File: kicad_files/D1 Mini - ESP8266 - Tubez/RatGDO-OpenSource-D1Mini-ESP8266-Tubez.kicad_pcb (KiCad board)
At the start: 2 copper layers, 51.8 x 65.8 mm, 24 parts, among them J1 Screw_Terminal_01x03, J2 Conn_01x11, J3 Screw_Terminal_01x02, Q1 2N7002, Q2 AO3400A, Q3 AO3400A, Q4 AO3400A, U1 WeMos_D1_mini, U2 K7805-500R3

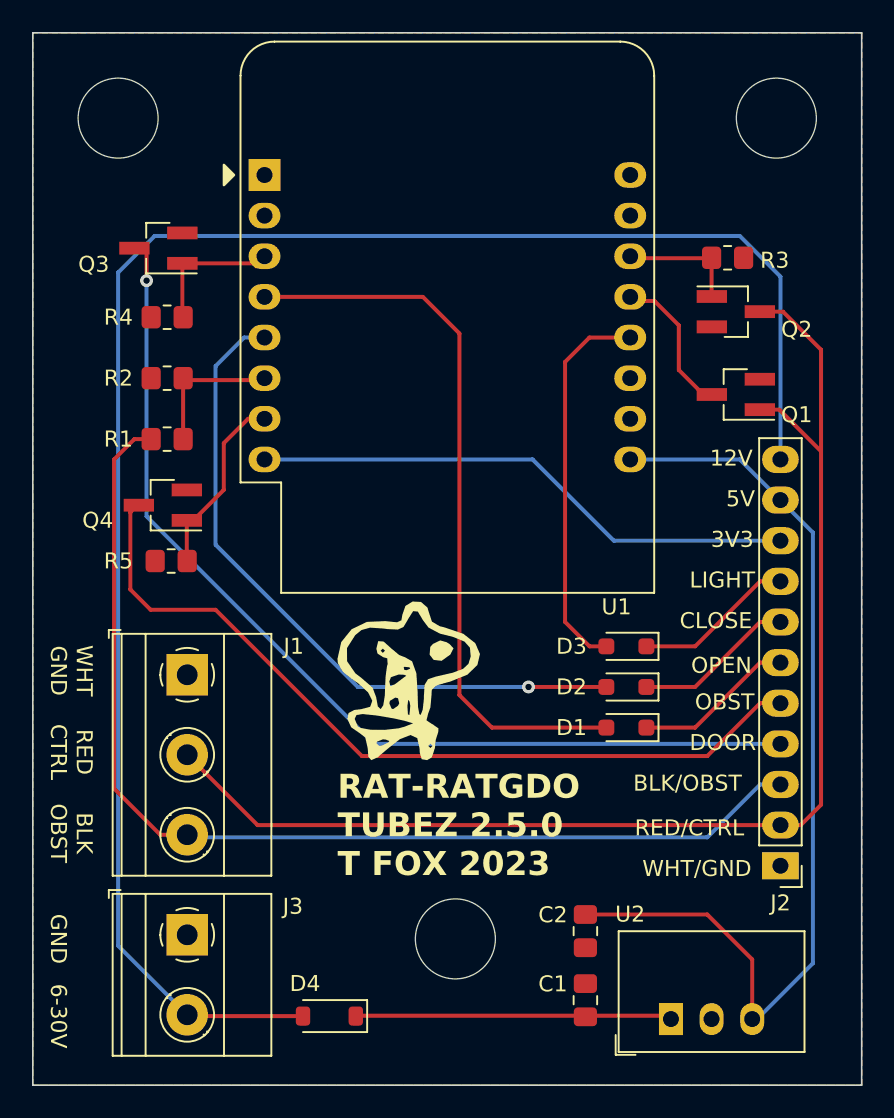
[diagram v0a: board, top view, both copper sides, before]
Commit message: Change angled track intersection to 90
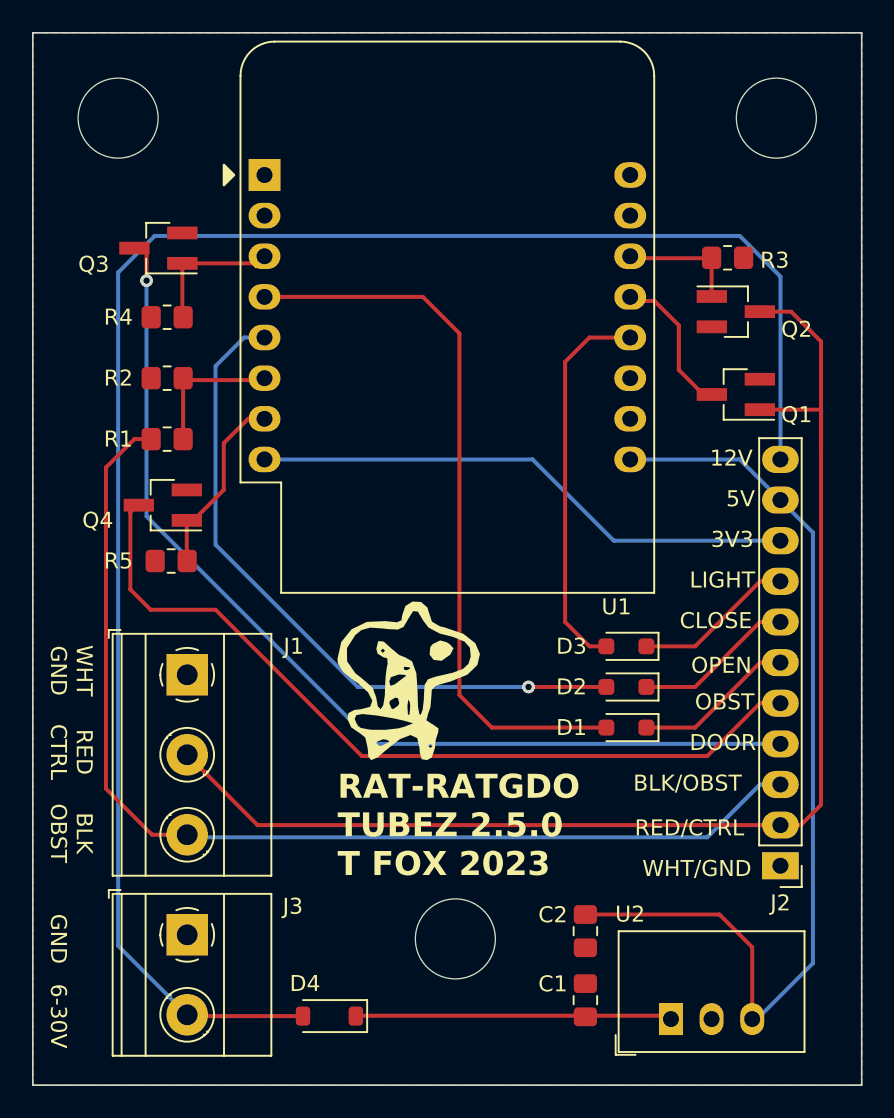
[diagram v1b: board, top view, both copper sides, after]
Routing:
- net RED/CTRL: track 81.3 -> 83.1 mm
- net BLK/OBST: track 65.7 -> 66.4 mm

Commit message: Update with potential three new v2.5 resistors.
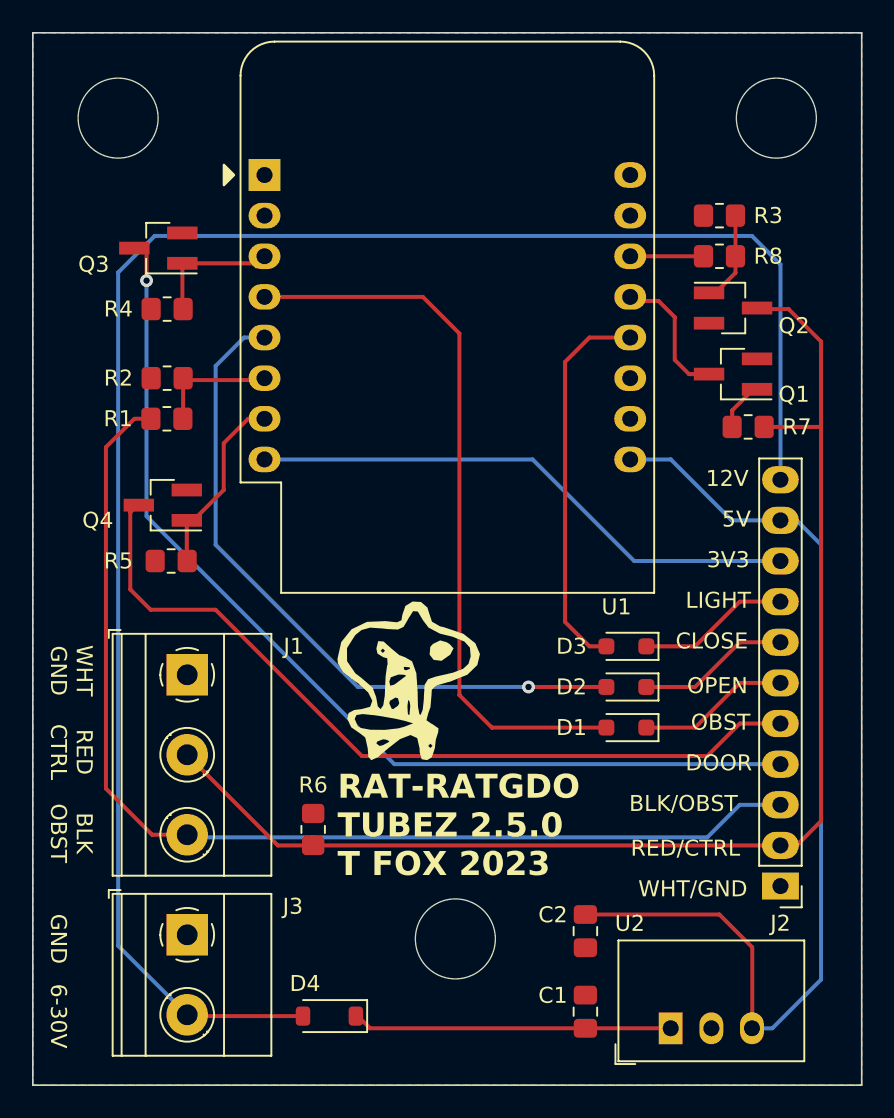
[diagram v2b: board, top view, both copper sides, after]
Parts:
- added R6: 10k, Resistor_SMD:R_0805_2012Metric_Pad1.20x1.40mm_HandSolder, F.Cu at (132.6, 107.0)
- added R7: 10k, Resistor_SMD:R_0805_2012Metric_Pad1.20x1.40mm_HandSolder, F.Cu at (159.8, 81.8)
- added R8: 1k, Resistor_SMD:R_0805_2012Metric_Pad1.20x1.40mm_HandSolder, F.Cu at (158.0, 71.1)
- moved R3 2.68 mm to (158.0, 68.6), turned to 180 degrees
- moved Q1 1.28 mm to (158.8, 78.5)
- moved R1 1.27 mm to (123.4, 81.3)
- moved J2 1.27 mm to (161.8, 110.5)
- moved C1 0.72 mm to (149.6, 118.3)
- moved U2 0.58 mm to (160.0, 119.4)
- moved R4 0.51 mm to (123.5, 74.4)
- moved Q2 0.28 mm to (158.8, 74.4)
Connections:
- Q1 pad 1: RED/CTRL -> Net-(Q1-G)
- Q2 pad 1: /ESP_TX -> Net-(Q2-G)
- R3 pad 1: /ESP_TX -> Net-(Q2-G)
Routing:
- net Net-(Q2-G): track 0.00 -> 5.65 mm
- net RED/CTRL: track 83.1 -> 79.4 mm
- net /ESP_TX: track 7.70 -> 4.58 mm
- net Net-(Q1-G): track 0.00 -> 2.98 mm
- net +12V: track 109.9 -> 111.6 mm
- net Net-(U1-MOSI/D7): track 9.14 -> 7.85 mm
- net DC_OPEN: track 10.1 -> 9.03 mm
- net STS_OBST: track 51.8 -> 50.7 mm
- net DC_LIGHT: track 10.1 -> 9.03 mm
- net DC_CLOSE: track 10.1 -> 9.03 mm
- net STS_DOOR: track 62.0 -> 62.5 mm

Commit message: addition of LEDs
work in progress
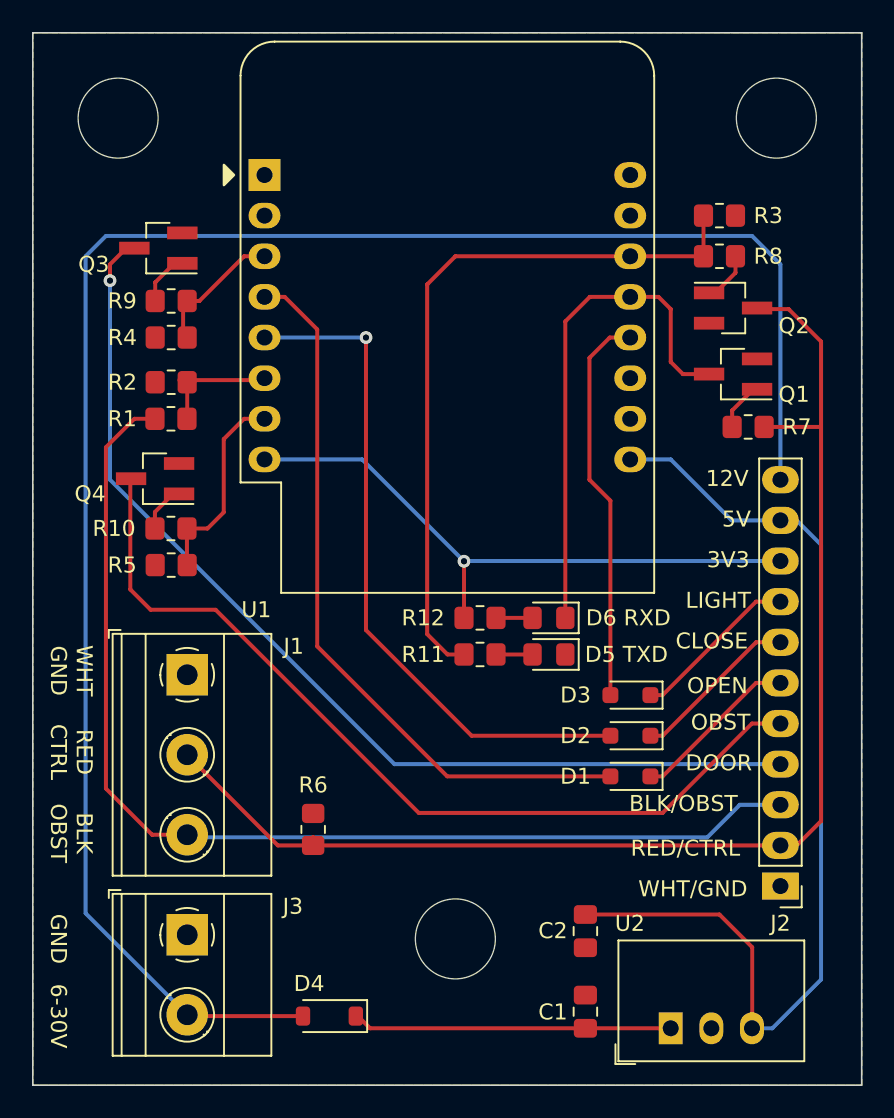
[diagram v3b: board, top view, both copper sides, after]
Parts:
- added D5 TXD: TX LED, LED_SMD:LED_0805_2012Metric_Pad1.15x1.40mm_HandSolder, F.Cu at (147.3, 96.0)
- added D6 RXD: RX LED, LED_SMD:LED_0805_2012Metric_Pad1.15x1.40mm_HandSolder, F.Cu at (147.3, 93.7)
- added R10: 1k, Resistor_SMD:R_0805_2012Metric_Pad1.20x1.40mm_HandSolder, F.Cu at (123.7, 88.1)
- added R11: 1k, Resistor_SMD:R_0805_2012Metric_Pad1.20x1.40mm_HandSolder, F.Cu at (143.0, 96.0)
- added R12: 1k, Resistor_SMD:R_0805_2012Metric_Pad1.20x1.40mm_HandSolder, F.Cu at (143.0, 93.7)
- added R9: 1k, Resistor_SMD:R_0805_2012Metric_Pad1.20x1.40mm_HandSolder, F.Cu at (123.7, 73.9)
- G***: moved to B.Cu
- moved G*** 6.76 mm to (144.0, 93.7), turned to 180 degrees
- moved D1 3.06 mm to (152.4, 103.6)
- moved D2 3.06 mm to (152.4, 101.1)
- moved D3 3.06 mm to (152.4, 98.6)
- moved R4 1.80 mm to (123.7, 76.2)
- moved Q4 1.73 mm to (122.7, 85.0)
- moved R2 0.36 mm to (123.7, 79.0)
- moved R5 0.25 mm to (123.7, 90.4)
- moved R1 0.25 mm to (123.7, 81.3)
- turned R3 to 0 degrees
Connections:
- R3 pad 1: Net-(Q2-G) -> /ESP_TX
- R4 pad 1: Net-(Q3-G) -> Net-(U1-D0)
- R5 pad 1: Net-(Q4-G) -> Net-(U1-CS/D8)
- U1 pad 3: Net-(Q3-G) -> Net-(U1-D0)
- U1 pad 7: Net-(Q4-G) -> Net-(U1-CS/D8)
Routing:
- net /ESP_TX: track 4.58 -> 45.2 mm
- net /ESP_RX: track 8.29 -> 31.5 mm
- net Net-(U1-CS/D8): track 0.00 -> 12.6 mm
- net Net-(Q4-G): track 11.3 -> 2.63 mm
- net Net-(U1-D0): track 0.00 -> 8.51 mm
- net Net-(Q3-G): track 9.03 -> 2.85 mm
- net STS_OBST: track 50.7 -> 55.3 mm
- net +3V3: track 34.4 -> 38.4 mm, vias 0 -> 1
- net +12V: track 111.6 -> 115.1 mm
- net Net-(Q2-G): track 5.65 -> 3.13 mm
- net Net-(D6-A): track 0.00 -> 2.28 mm
- net Net-(D5-A): track 0.00 -> 2.28 mm
- net STS_DOOR: track 62.5 -> 63.8 mm
- net DC_OPEN: track 9.03 -> 10.0 mm
- net DC_LIGHT: track 9.03 -> 10.0 mm
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
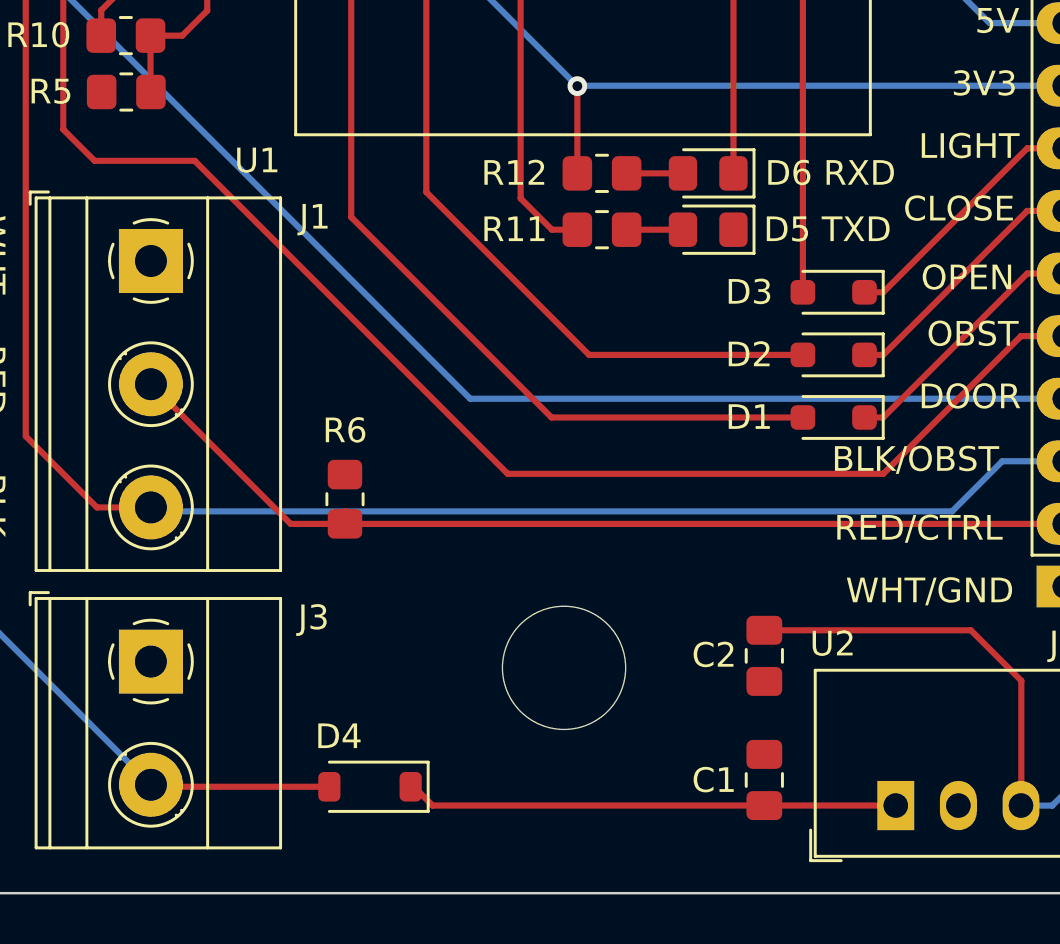
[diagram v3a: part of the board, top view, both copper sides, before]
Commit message: Add 750mA fuse
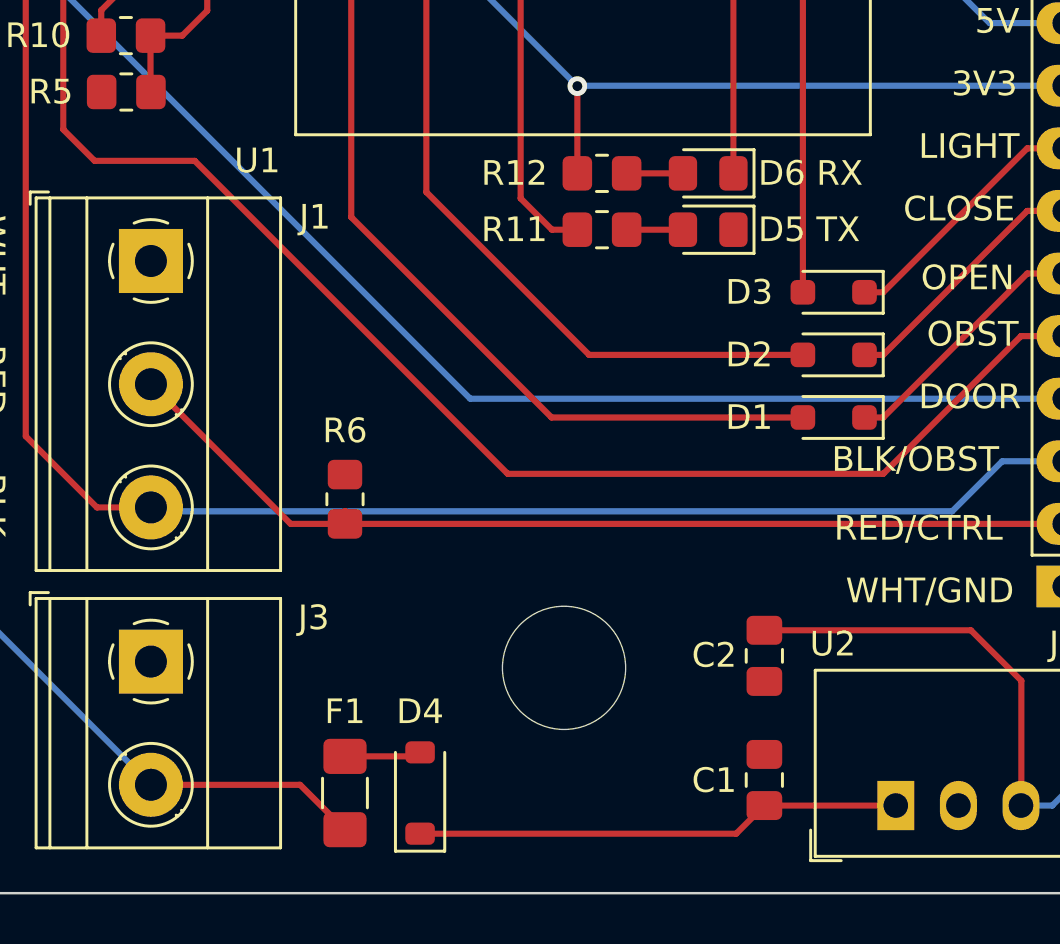
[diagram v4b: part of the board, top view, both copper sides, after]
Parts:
- added F1: 750mA, Fuse:Fuse_1206_3216Metric_Pad1.42x1.75mm_HandSolder, F.Cu at (132.6, 118.9)
- D5 TX: renamed from D5 TXD
- D6 RX: renamed from D6 RXD
- moved D4 2.05 mm to (135.6, 118.9), turned to 90 degrees
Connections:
- D4 pad 2: +12V -> Net-(D4-A)
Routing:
- net Net-(D4-A): track 0.00 -> 2.89 mm
- net +12V: track 115.1 -> 116.8 mm

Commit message: Silkscreen change
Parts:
- moved G*** 3.56 mm to (140.5, 93.7)
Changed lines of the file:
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@@
   )
   (footprint "LOGO" (layer "B.Cu")
-    (at 144.018 93.726 180)
+    (at 140.462 93.726 180)
     (attr board_only exclude_from_pos_files exclude_from_bom)
     (fp_text reference "G***" (at 0 0) (layer "F.SilkS") hide

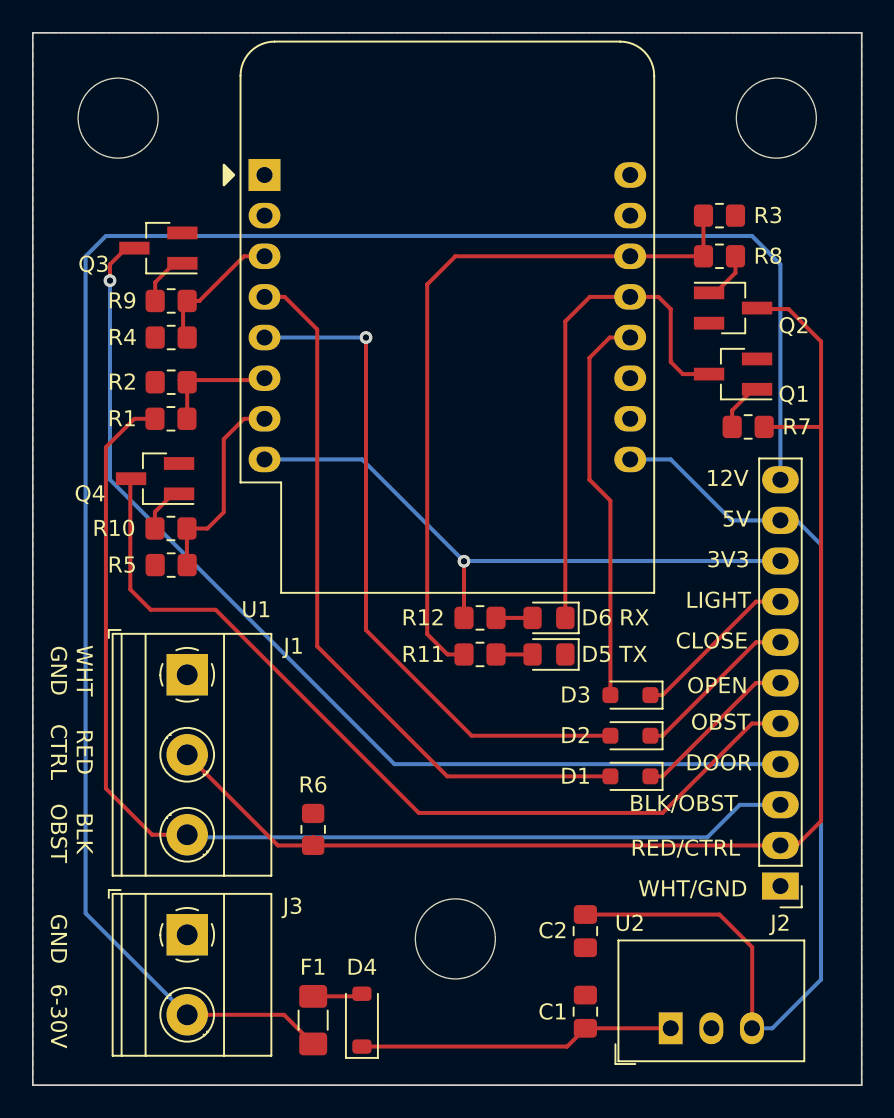
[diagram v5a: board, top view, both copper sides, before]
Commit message: Added smt pcb jumper to switch between 5V or 3v3 supply
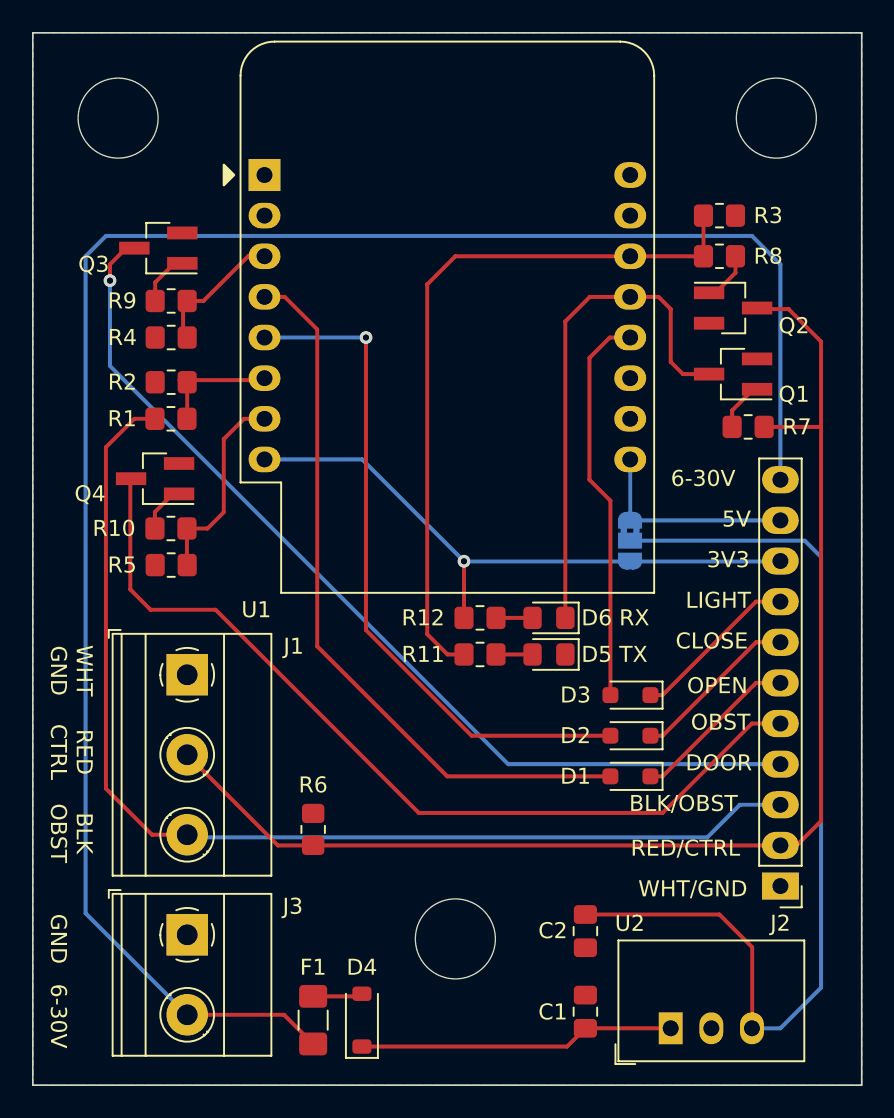
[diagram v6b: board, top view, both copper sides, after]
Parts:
- added JP1: Jumper_3_Bridged12, Jumper:SolderJumper-3_P1.3mm_Bridged2Bar12_RoundedPad1.0x1.5mm, B.Cu at (152.4, 88.9)
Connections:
- C2 pad 1: +5V -> Net-(JP1-C)
- U2 pad 3: +5V -> Net-(JP1-C)
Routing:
- net Net-(JP1-C): track 0.00 -> 60.7 mm
- net +5V: track 61.4 -> 13.1 mm
- net STS_DOOR: track 63.8 -> 59.6 mm
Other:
- board text removed: "12V"

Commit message: Silkscreen cleanup
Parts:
- moved G*** 0.76 mm to (140.5, 94.5)
